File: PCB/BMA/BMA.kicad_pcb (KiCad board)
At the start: 2 copper layers, 91.4 x 134.6 mm, 26 parts, among them J1 Conn_01x15, J10 Conn_01x10, J11 Conn_01x05, J12 Conn_01x04, J13 Conn_01x05, J14 Conn_01x05, J2 Conn_01x02, J3 Conn_01x02, J4 Conn_01x05, J5 Conn_01x05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

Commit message: Some progress
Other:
- board text added: "3V GND"
- board text added: "5V GND"
- board text added: "ADS1115-1"
- board text added: "ADS1115-2"
- board text added: "AM-1"
- board text added: "AM-2"
- board text added: "AM-3"
- board text added: "AM-4"
- board text added: "AM-5"
- board text added: "AM-6"
- board text added: "SENSOR"
- board text added: "TCA9548A"
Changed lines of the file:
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@@
       (outputformat 1)
       (mirror false)
-      (drillshape 1)
+      (drillshape 0)
       (scaleselection 1)
-      (outputdirectory "")
+      (outputdirectory "../BMA_Gerber/")
     )
   )
@@
     (property "Sheetname" "")
     (attr through_hole)
-    (fp_text reference "J5" (at 0 -2.33) (layer "F.SilkS")
+    (fp_text reference "J5" (at 0 -2.33) (layer "F.SilkS") hide
       (effects (font (size 1 1) (thickness 0.15)))
     )
@@
     (property "Sheetname" "")
     (attr through_hole)
-    (fp_text reference "J11" (at 0 -2.33) (layer "F.SilkS")
+    (fp_text reference "J11" (at 0 -2.33) (layer "F.SilkS") hide
       (effects (font (size 1 1) (thickness 0.15)))
     )
@@
     (property "Sheetname" "")
     (attr through_hole)
-    (fp_text reference "J4" (at 0 -2.33) (layer "F.SilkS")
+    (fp_text reference "J4" (at 0 -2.33) (layer "F.SilkS") hide
       (effects (font (size 1 1) (thickness 0.15)))
     )
@@
     (property "Sheetname" "")
     (attr through_hole)
-    (fp_text reference "J8" (at 0 -2.33) (layer "F.SilkS")
+    (fp_text reference "J8" (at 0 -2.33) (layer "F.SilkS") hide
       (effects (font (size 1 1) (thickness 0.15)))
     )
@@
     (property "Sheetname" "")
     (attr through_hole)
-    (fp_text reference "J13" (at 0 -2.33) (layer "F.SilkS")
+    (fp_text reference "J13" (at 0 -2.33) (layer "F.SilkS") hide
       (effects (font (size 1 1) (thickness 0.15)))
     )
@@
     (property "Sheetname" "")
     (attr through_hole)
-    (fp_text reference "J14" (at 0 -2.33) (layer "F.SilkS")
+    (fp_text reference "J14" (at 0 -2.33) (layer "F.SilkS") hide
       (effects (font (size 1 1) (thickness 0.15)))
     )
@@
   )
   (gr_rect (start 45.72 157.48) (end 137.16 22.86) (layer "Edge.Cuts") (width 0.2) (fill none))
+  (gr_text "ADS1115-1" (at 110.49 87.63 90) (layer "F.SilkS")
+    (effects (font (size 1.5 1.5) (thickness 0.3)))
+  )
+  (gr_text "TCA9548A" (at 110.49 49.53 90) (layer "F.SilkS")
+    (effects (font (size 1.5 1.5) (thickness 0.3)))
+  )
+  (gr_text "5V GND" (at 115.57 31.75) (layer "F.SilkS")
+    (effects (font (size 1.5 1.5) (thickness 0.3)))
+  )
+  (gr_text "AM-2" (at 54.61 59.69 90) (layer "F.SilkS")
+    (effects (font (size 1.5 1.5) (thickness 0.3)))
+  )
+  (gr_text "AM-6" (at 54.61 140.97 90) (layer "F.SilkS")
+    (effects (font (size 1.5 1.5) (thickness 0.3)))
+  )
+  (gr_text "AM-4\n" (at 54.61 100.33 90) (layer "F.SilkS")
+    (effects (font (size 1.5 1.5) (thickness 0.3)))
+  )
+  (gr_text "ADS1115-2" (at 110.49 118.11 90) (layer "F.SilkS")
+    (effects (font (size 1.5 1.5) (thickness 0.3)))
+  )
+  (gr_text "AM-3" (at 54.61 80.01 90) (layer "F.SilkS")
+    (effects (font (size 1.5 1.5) (thickness 0.3)))
+  )
+  (gr_text "AM-1" (at 54.61 39.37 90) (layer "F.SilkS")
+    (effects (font (size 1.5 1.5) (thickness 0.3)))
+  )
+  (gr_text "AM-5" (at 54.61 120.65 90) (layer "F.SilkS")
+    (effects (font (size 1.5 1.5) (thickness 0.3)))
+  )
+  (gr_text "SENSOR" (at 110.49 149.86 90) (layer "F.SilkS")
+    (effects (font (size 1.5 1.5) (thickness 0.3)))
+  )
+  (gr_text "3V GND" (at 105.41 31.75) (layer "F.SilkS")
+    (effects (font (size 1.5 1.5) (thickness 0.3)))
+  )
   (segment (start 112.6999 114.1957) (end 114.0792 115.575) (width 1) (layer "F.Cu") (net 1))
   (segment (start 89.8925 62.0401) (end 91.9239 64.0715) (width 1) (layer "F.Cu") (net 1))

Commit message: POC 4
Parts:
- moved K1 43.4 mm to (92.4, 85.4)
- moved J10 43.4 mm to (129.5, 153.7)
- moved J13 43.4 mm to (66.0, 160.0)
- moved J14 43.4 mm to (66.0, 180.3)
- moved K11 43.4 mm to (92.4, 188.0)
- moved K12 43.4 mm to (103.1, 188.0)
- moved J5 43.4 mm to (66.0, 99.1)
- moved J8 43.4 mm to (66.0, 119.4)
- moved K2 43.4 mm to (103.1, 85.4)
- moved K3 43.4 mm to (92.4, 106.7)
- moved K5 43.4 mm to (92.4, 127.0)
- moved J1 43.4 mm to (73.7, 68.6)
- moved J2 43.4 mm to (119.4, 68.6)
- moved J3 43.4 mm to (129.5, 68.6)
- moved J4 43.4 mm to (66.0, 78.7)
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
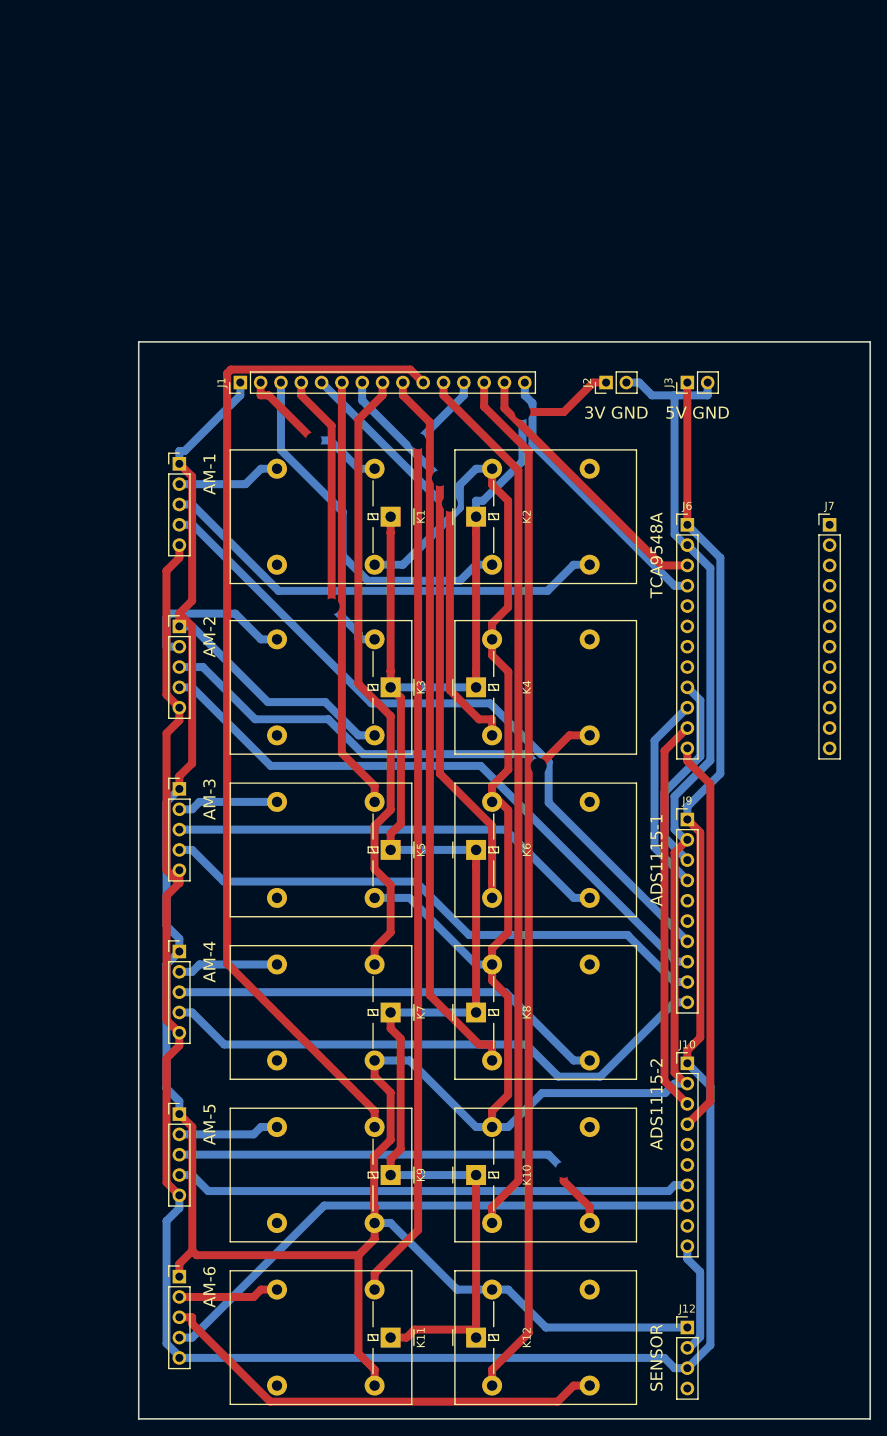
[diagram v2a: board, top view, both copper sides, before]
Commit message: Fixed drill size for vias
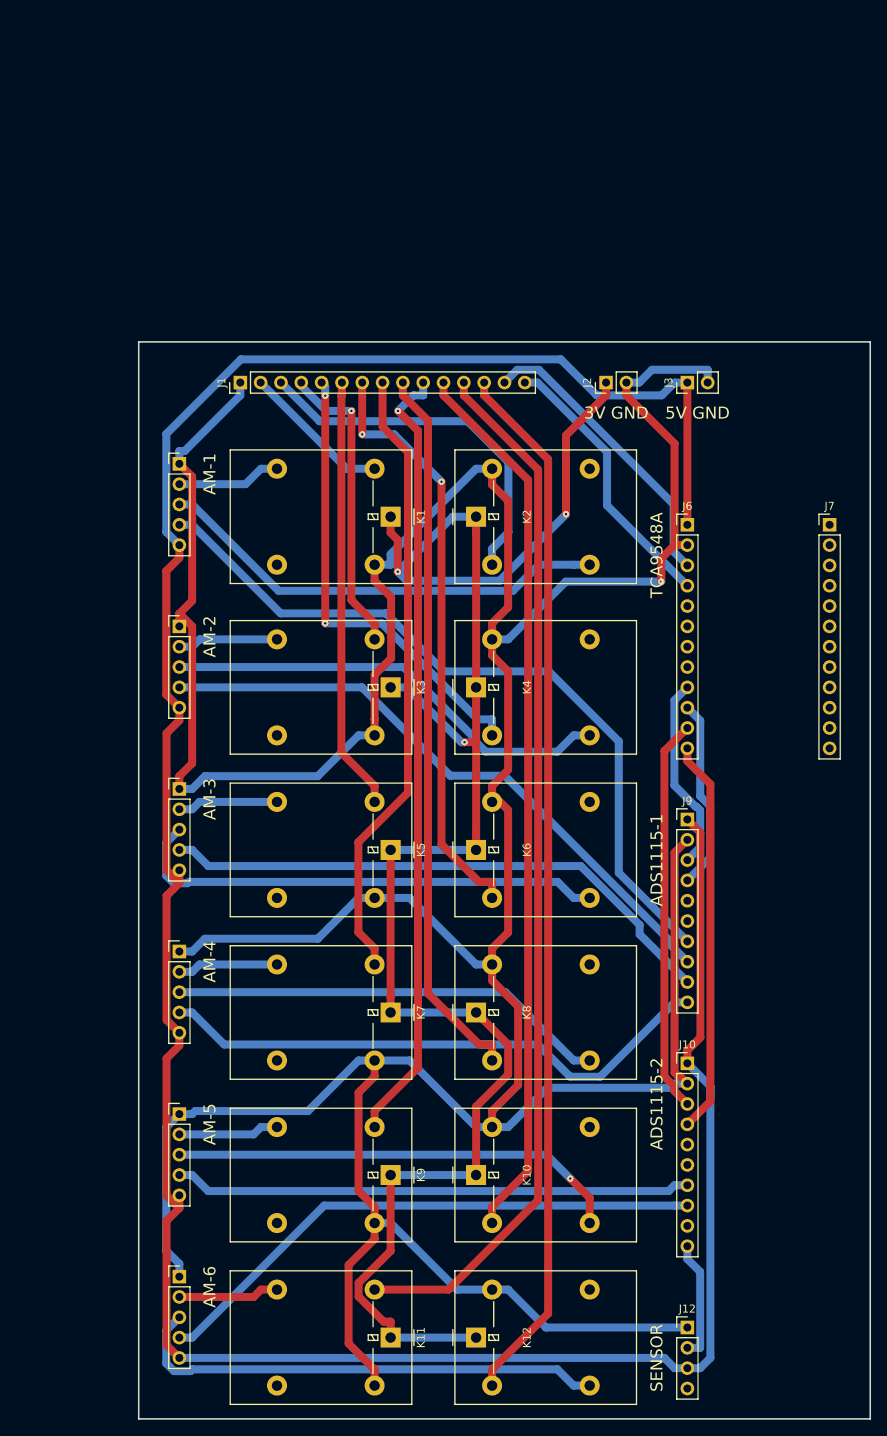
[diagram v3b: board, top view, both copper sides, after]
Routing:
- net Net-(J10-Pad1): track 304.3 -> 352.6 mm
- net Net-(J1-Pad10): track 127.2 -> 98.3 mm, vias 0 -> 1
- net Net-(J2-Pad1): track 207.9 -> 229.4 mm, vias 1 -> 3
- net Net-(J1-Pad12): track 118.0 -> 131.1 mm, vias 1 -> 0
- net Net-(J5-Pad2): track 20.6 -> 12.6 mm
- net Net-(J4-Pad4): track 88.1 -> 94.7 mm
- net Net-(J8-Pad3): track 54.8 -> 60.7 mm
- net Net-(J1-Pad1): track 542.1 -> 546.8 mm, vias 0 -> 1
- net Net-(J14-Pad3): track 57.0 -> 60.7 mm
- net Net-(J1-Pad5): track 54.4 -> 58.1 mm, vias 1 -> 2
- net Net-(J1-Pad7): track 71.1 -> 74.4 mm, vias 1 -> 2
- net Net-(J1-Pad14): track 34.2 -> 37.1 mm
- net Net-(J1-Pad13): track 129.6 -> 131.6 mm
- net Net-(J5-Pad3): track 58.0 -> 56.7 mm, vias 1 -> 0
- net Net-(J6-Pad10): track 25.0 -> 24.0 mm
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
